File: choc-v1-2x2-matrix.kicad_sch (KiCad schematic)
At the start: 5 parts

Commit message: this is looking good thus far
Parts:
- added C?: 10uF, symbol Device:C_Small
- added C? (x3): 0.1uF, symbol Device:C_Small
- added C? (x2): 22pF, symbol Device:C_Small
- added F?: Polyfuse_Small, symbol Device:Polyfuse_Small
- added R?: 10k, symbol Device:R_Small
- added SW?: SW_Push, symbol Switch:SW_Push
- added USB?: Molex-0548190589, symbol random-keyboard-parts:Molex-0548190589
- added Y?: Crystal_GND24_Small, symbol Device:Crystal_GND24_Small
- C?: value C_Small -> 1uF
- R? (x2): value R_Small -> 22
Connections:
- net +5V: now also U?.7 (VBUS), C?.1, C?.1, C?.1, C?.1, F?.2, R?.1
- net GND: now also C?.1, C?.1, C?.2, C?.2, C?.2, C?.2, SW?.1, USB?.1 (GND), Y?.1, Y?.3
- net D+: now reaches R?.2
- net D+: now also USB?.3 (D+)
- net at U?.13 (~{RESET}): now also R?.2, SW?.2
- net at U?.16 (XTAL2): now also C?.2, Y?.2
- net at U?.17 (XTAL1): now also C?.2, Y?.4
- net D-: now reaches R?.1
- net D-: now also USB?.4 (D-)
- new net VCC: F?.1, USB?.5 (VBUS)

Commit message: finished schematic?
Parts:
- added D? (x4): D_Small, symbol Device:D_Small
- added MX? (x4): MX-NoLED, symbol MX_Alps_Hybrid:MX-NoLED
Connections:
- new net: D?.2 (A), MX?.2 (ROW) (x4)
- new net COL0: MX?.1 (COL), MX?.1 (COL)
- new net COL1: MX?.1 (COL), MX?.1 (COL)
- new net ROW0: D?.1 (K), D?.1 (K)
- new net ROW1: D?.1 (K), D?.1 (K)

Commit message: working on the footprint placement
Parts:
- C1, C2, C3, C4, C5, C6, C7: renamed from C?; footprint (none) -> Capacitor_SMD:C_0805_2012Metric_Pad1.18x1.45mm_HandSolder
- D1, D2, D3, D4: renamed from D?; footprint (none) -> Diode_SMD:D_SOD-123
- F1: renamed from F?; value Polyfuse_Small -> 500mA; footprint (none) -> Fuse:Fuse_0805_2012Metric_Pad1.15x1.40mm_HandSolder
- MX1, MX2, MX3, MX4: renamed from MX?; footprint (none) -> MX_Alps_Hybrid:MX-1.5U-NoLED
- R1, R2, R3, R4: renamed from R?; footprint (none) -> Resistor_SMD:R_0805_2012Metric_Pad1.20x1.40mm_HandSolder
- SW1: renamed from SW?; footprint (none) -> random-keyboard-parts:SKQG-1155865
- USB1: renamed from USB?; footprint (none) -> random-keyboard-parts:Molex-0548190589
- Y1: renamed from Y?; footprint (none) -> Crystal:Crystal_SMD_3225-4Pin_3.2x2.5mm_HandSoldering
- gave numbers to parts that had none: 1
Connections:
- net GND: now also USB1.6 (SHIELD)
- no-connect marks 0 -> 27
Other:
- moved on the sheet: C1, C2, C3, C4, D1, D2, D3, D4, F1, MX1, MX2, MX3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

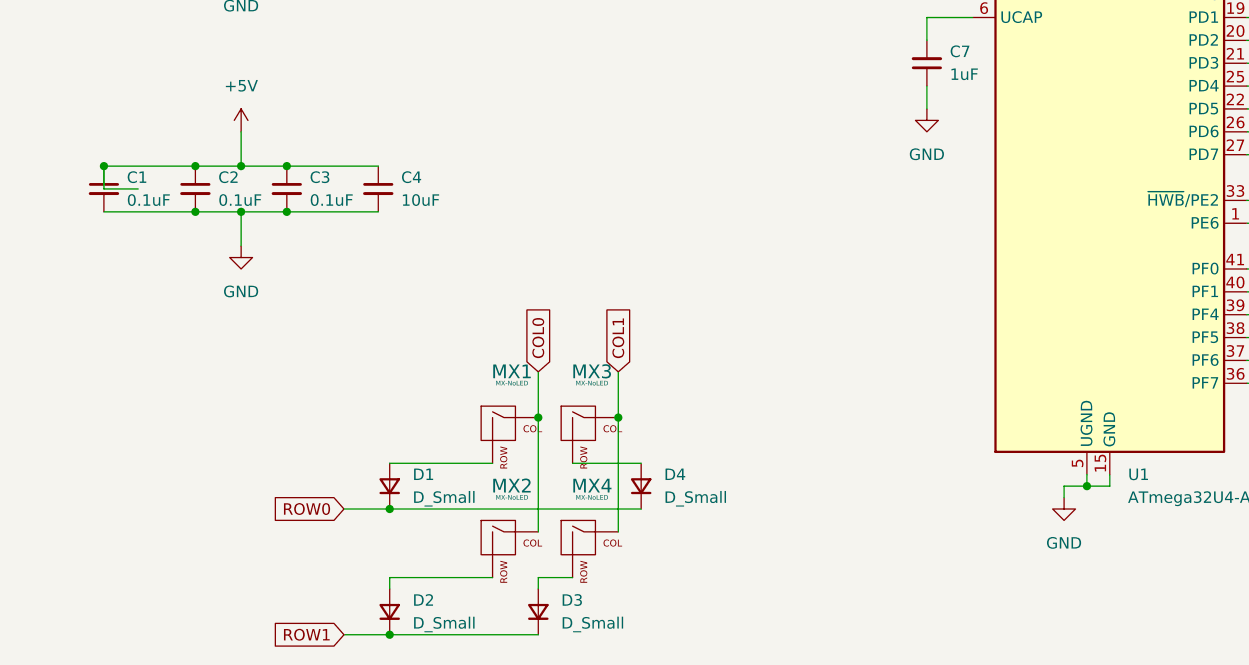
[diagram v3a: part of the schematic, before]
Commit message: still working on the footprint placement
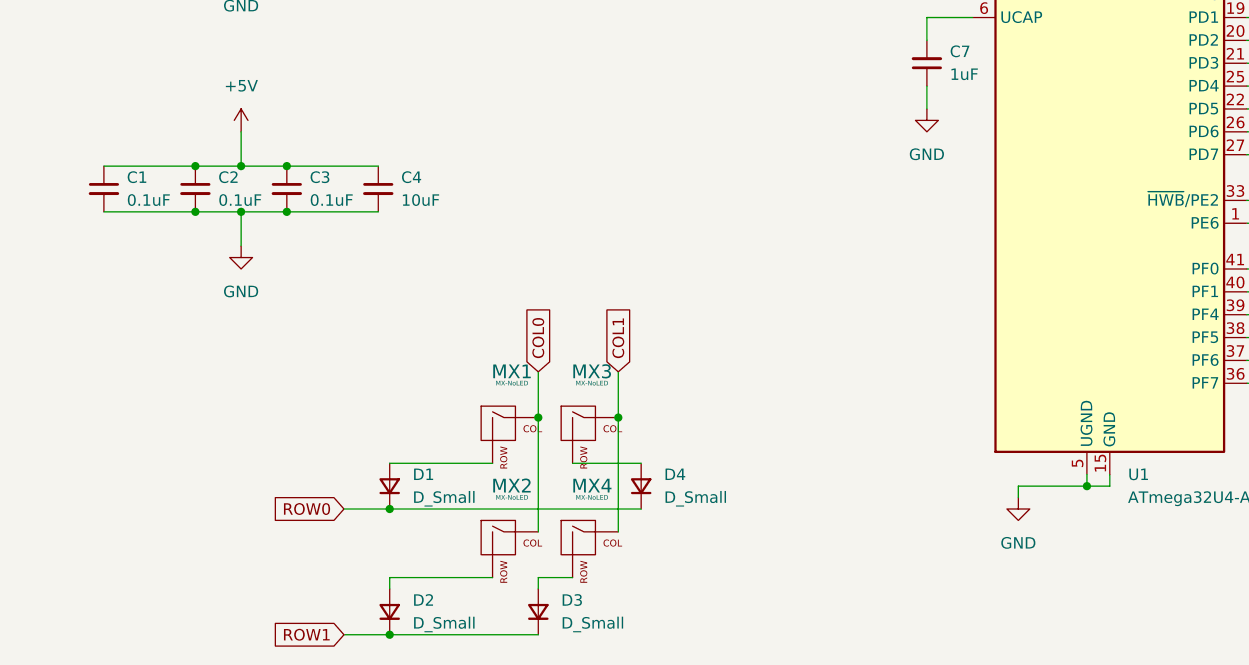
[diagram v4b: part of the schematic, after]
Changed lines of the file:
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@@
   (junction (at 73.66 95.25) (diameter 0) (color 0 0 0 0)
-  )
-  (junction (at 63.5 95.25) (diameter 0) (color 0 0 0 0)
   )
   (junction (at 120.65 123.19) (diameter 0) (color 0 0 0 0)
@@
     (stroke (width 0) (type default) (color 0 0 0 0))
   )
-  (wire (pts (xy 172.72 130.81) (xy 170.18 130.81))
+  (wire (pts (xy 172.72 130.81) (xy 165.1 130.81))
     (stroke (width 0) (type default) (color 0 0 0 0))
   )
@@
     (stroke (width 0) (type default) (color 0 0 0 0))
   )
-  (wire (pts (xy 63.5 97.79) (xy 63.5 95.25))
-    (stroke (width 0) (type default) (color 0 0 0 0))
-  )
   (wire (pts (xy 175.26 35.56) (xy 177.8 35.56))
     (stroke (width 0) (type default) (color 0 0 0 0))
@@
     (stroke (width 0) (type default) (color 0 0 0 0))
   )
-  (wire (pts (xy 170.18 130.81) (xy 170.18 132.08))
-    (stroke (width 0) (type default) (color 0 0 0 0))
-  )
-  (wire (pts (xy 67.31 97.79) (xy 63.5 97.79))
+  (wire (pts (xy 165.1 130.81) (xy 165.1 132.08))
     (stroke (width 0) (type default) (color 0 0 0 0))
   )
@@
     (pin "4")
   )
-  (symbol (lib_id "power:GND") (at 170.18 132.08 0) (unit 1)
+  (symbol (lib_id "power:GND") (at 165.1 132.08 0) (unit 1)
     (in_bom yes) (on_board yes) (fields_autoplaced)
-    (property "Reference" "#PWR0112" (id 0) (at 170.18 138.43 0)
+    (property "Reference" "#PWR0112" (id 0) (at 165.1 138.43 0)
       (effects (font (size 1.27 1.27)) hide)
     )
-    (property "Value" "GND" (id 1) (at 170.18 137.16 0))
-    (property "Footprint" "" (id 2) (at 170.18 132.08 0)
+    (property "Value" "GND" (id 1) (at 165.1 137.16 0))
+    (property "Footprint" "" (id 2) (at 165.1 132.08 0)
       (effects (font (size 1.27 1.27)) hide)
     )
-    (property "Datasheet" "" (id 3) (at 170.18 132.08 0)
+    (property "Datasheet" "" (id 3) (at 165.1 132.08 0)
       (effects (font (size 1.27 1.27)) hide)
     )
